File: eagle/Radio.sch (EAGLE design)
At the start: 105 parts, among them J500 2060-402, J501 2060-402, J920 2060-402, J921 2060-402, Q210 32.768kHz, Q610 32.768kHz, Q900 BSS123, U100 LP38693, U200 MSP430G2553, U300 IRF7103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

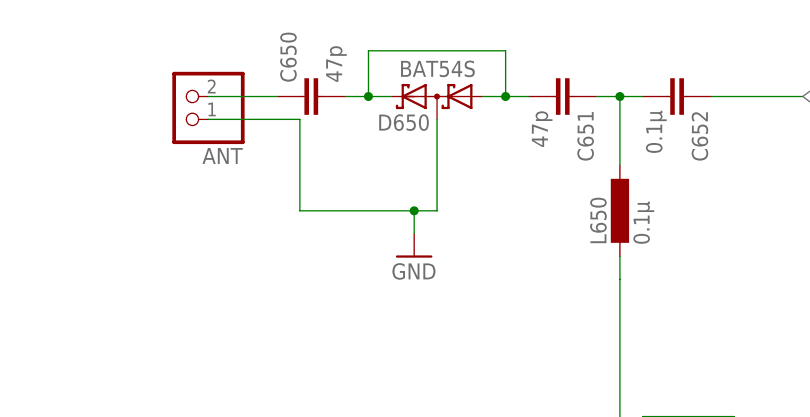
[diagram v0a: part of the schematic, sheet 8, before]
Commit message: CHG: eagle schemetics and layout to solve issue with diode on antenna
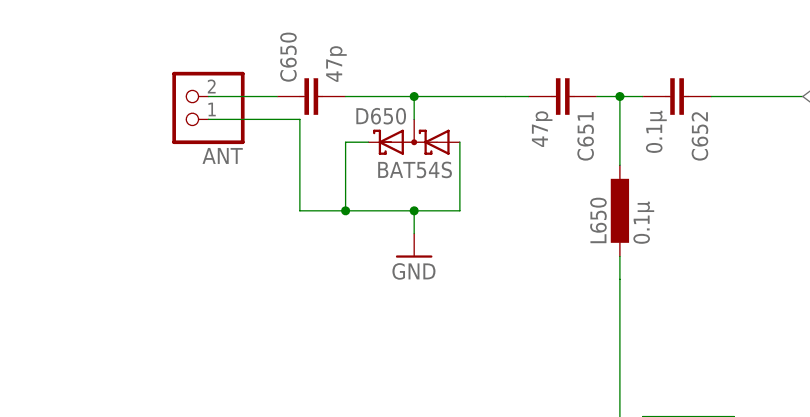
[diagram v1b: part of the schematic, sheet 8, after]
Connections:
- net GND: now also D650.A1, D650.C2; no longer D650.C1A2
- net N$2: now also D650.C1A2; no longer D650.A1, D650.C2
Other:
- moved on the sheet: D650
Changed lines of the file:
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@@
 <instance part="FRAME10" gate="G$1" x="0" y="0"/>
 <instance part="GND24" gate="1" x="167.64" y="93.98"/>
-<instance part="D650" gate="G$1" x="134.62" y="142.24" rot="R180"/>
+<instance part="D650" gate="G$1" x="132.08" y="137.16" rot="MR0"/>
 <instance part="ANT" gate="G$1" x="106.68" y="142.24" rot="R180"/>
 <instance part="C655" gate="G$1" x="165.1" y="78.74" rot="R270"/>
@@
 <net name="N$2" class="0">
 <segment>
+<pinref part="C651" gate="G$1" pin="2"/>
+<wire x1="144.78" y1="142.24" x2="142.24" y2="142.24" width="0.1524" layer="91"/>
 <pinref part="C650" gate="G$1" pin="2"/>
-<pinref part="D650" gate="G$1" pin="C2"/>
-<wire x1="124.46" y1="142.24" x2="127" y2="142.24" width="0.1524" layer="91"/>
-<wire x1="127" y1="142.24" x2="129.54" y2="142.24" width="0.1524" layer="91"/>
-<wire x1="127" y1="142.24" x2="127" y2="147.32" width="0.1524" layer="91"/>
-<junction x="127" y="142.24"/>
-<pinref part="C651" gate="G$1" pin="2"/>
-<pinref part="D650" gate="G$1" pin="A1"/>
-<wire x1="144.78" y1="142.24" x2="142.24" y2="142.24" width="0.1524" layer="91"/>
-<wire x1="142.24" y1="142.24" x2="139.7" y2="142.24" width="0.1524" layer="91"/>
-<wire x1="127" y1="147.32" x2="142.24" y2="147.32" width="0.1524" layer="91"/>
-<wire x1="142.24" y1="147.32" x2="142.24" y2="142.24" width="0.1524" layer="91"/>
-<junction x="142.24" y="142.24"/>
+<pinref part="D650" gate="G$1" pin="C1A2"/>
+<wire x1="124.46" y1="142.24" x2="132.08" y2="142.24" width="0.1524" layer="91"/>
+<wire x1="132.08" y1="142.24" x2="132.08" y2="139.7" width="0.1524" layer="91"/>
+<wire x1="142.24" y1="142.24" x2="132.08" y2="142.24" width="0.1524" layer="91"/>
+<junction x="132.08" y="142.24"/>
 </segment>
 </net>
@@
 </segment>
 <segment>
-<pinref part="D650" gate="G$1" pin="C1A2"/>
-<wire x1="134.62" y1="139.7" x2="134.62" y2="129.54" width="0.1524" layer="91"/>
 <pinref part="GND37" gate="1" pin="GND"/>
-<wire x1="134.62" y1="129.54" x2="132.08" y2="129.54" width="0.1524" layer="91"/>
 <wire x1="132.08" y1="129.54" x2="132.08" y2="127" width="0.1524" layer="91"/>
 <pinref part="ANT" gate="G$1" pin="1"/>
 <wire x1="119.38" y1="139.7" x2="109.22" y2="139.7" width="0.1524" layer="91"/>
 <wire x1="119.38" y1="139.7" x2="119.38" y2="129.54" width="0.1524" layer="91"/>
-<wire x1="119.38" y1="129.54" x2="132.08" y2="129.54" width="0.1524" layer="91"/>
+<wire x1="119.38" y1="129.54" x2="124.46" y2="129.54" width="0.1524" layer="91"/>
+<pinref part="D650" gate="G$1" pin="C2"/>
+<wire x1="124.46" y1="129.54" x2="132.08" y2="129.54" width="0.1524" layer="91"/>
+<wire x1="127" y1="137.16" x2="124.46" y2="137.16" width="0.1524" layer="91"/>
+<wire x1="124.46" y1="137.16" x2="124.46" y2="129.54" width="0.1524" layer="91"/>
+<junction x="124.46" y="129.54"/>
+<pinref part="D650" gate="G$1" pin="A1"/>
+<wire x1="137.16" y1="137.16" x2="137.16" y2="129.54" width="0.1524" layer="91"/>
+<wire x1="137.16" y1="129.54" x2="132.08" y2="129.54" width="0.1524" layer="91"/>
 <junction x="132.08" y="129.54"/>
 </segment>

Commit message: CHG: Finishing Layout and Schemetics
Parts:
- added R921, R922, R923: 1k, rcl:R-EU_R1206
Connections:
- new net N$25: R921.1, U920.LED1
- new net N$45: J920.B-2, R922.2
- new net N$46: J921.B-2, R923.2
- net +5V: no longer R901.1
- net GND: now also R901.1
- net N$3: now also R923.1, U920.LED3; no longer J920.B-1, U920.LED1
- net N$44: now also J920.B-1, R921.2; no longer J921.B-2, U920.LED3
- net N$5: now also R922.1; no longer J920.B-2
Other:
- moved on the sheet: J920, J921
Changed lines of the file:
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@@
 <part name="GND28" library="supply1" deviceset="GND" device=""/>
 <part name="R901" library="rcl" deviceset="R-EU_" device="R1206" value="1k"/>
-<part name="P+2" library="supply1" deviceset="+5V" device=""/>
 <part name="J501" library="Wago-2060-402" deviceset="2060-402" device=""/>
 <part name="J500" library="Wago-2060-402" deviceset="2060-402" device=""/>
@@
 <part name="J920" library="Wago-2060-402" deviceset="2060-402" device=""/>
 <part name="U940" library="Radio Projekt" deviceset="OPT3001" device=""/>
+<part name="GND25" library="supply1" deviceset="GND" device=""/>
+<part name="R921" library="rcl" deviceset="R-EU_" device="R1206" value="1k"/>
+<part name="R922" library="rcl" deviceset="R-EU_" device="R1206" value="1k"/>
+<part name="R923" library="rcl" deviceset="R-EU_" device="R1206" value="1k"/>
 </parts>
 <sheets>
@@
 <instance part="GND28" gate="1" x="137.16" y="104.14"/>
 <instance part="R901" gate="G$1" x="149.86" y="119.38" rot="R270"/>
-<instance part="P+2" gate="1" x="149.86" y="129.54"/>
-<instance part="J921" gate="A" x="101.6" y="30.48" rot="MR180"/>
-<instance part="P+4" gate="1" x="93.98" y="10.16" rot="R180"/>
+<instance part="J921" gate="A" x="116.84" y="30.48" rot="MR180"/>
+<instance part="P+4" gate="1" x="109.22" y="10.16" rot="R180"/>
 <instance part="C903" gate="G$1" x="127" y="142.24" rot="R90"/>
 <instance part="GND32" gate="1" x="139.7" y="142.24" rot="R90"/>
@@
 <instance part="U920" gate="G$1" x="68.58" y="43.18"/>
 <instance part="GND39" gate="1" x="45.72" y="27.94"/>
-<instance part="J920" gate="A" x="101.6" y="45.72"/>
+<instance part="J920" gate="A" x="116.84" y="45.72"/>
+<instance part="GND25" gate="1" x="149.86" y="129.54" rot="R180"/>
+<instance part="R921" gate="G$1" x="93.98" y="45.72"/>
+<instance part="R922" gate="G$1" x="101.6" y="38.1"/>
+<instance part="R923" gate="G$1" x="93.98" y="33.02"/>
 </instances>
 <busses>
@@
 <wire x1="45.72" y1="30.48" x2="45.72" y2="33.02" width="0.1524" layer="91"/>
 <wire x1="45.72" y1="33.02" x2="50.8" y2="33.02" width="0.1524" layer="91"/>
+</segment>
+<segment>
+<pinref part="R901" gate="G$1" pin="1"/>
+<wire x1="149.86" y1="124.46" x2="149.86" y2="127" width="0.1524" layer="91"/>
+<pinref part="GND25" gate="1" pin="GND"/>
 </segment>
 </net>
@@
 </segment>
 <segment>
-<pinref part="R901" gate="G$1" pin="1"/>
-<pinref part="P+2" gate="1" pin="+5V"/>
-<wire x1="149.86" y1="124.46" x2="149.86" y2="127" width="0.1524" layer="91"/>
-</segment>
-<segment>
-<wire x1="93.98" y1="15.24" x2="93.98" y2="12.7" width="0.1524" layer="91"/>
+<wire x1="109.22" y1="17.78" x2="109.22" y2="12.7" width="0.1524" layer="91"/>
 <pinref part="P+4" gate="1" pin="+5V"/>
-<wire x1="93.98" y1="25.4" x2="93.98" y2="30.48" width="0.1524" layer="91"/>
+<wire x1="109.22" y1="25.4" x2="109.22" y2="30.48" width="0.1524" layer="91"/>
 <pinref part="J921" gate="A" pin="B-1"/>
-<wire x1="96.52" y1="30.48" x2="93.98" y2="30.48" width="0.1524" layer="91"/>
-<wire x1="93.98" y1="15.24" x2="93.98" y2="25.4" width="0.1524" layer="91"/>
+<wire x1="111.76" y1="30.48" x2="109.22" y2="30.48" width="0.1524" layer="91"/>
+<wire x1="109.22" y1="17.78" x2="109.22" y2="25.4" width="0.1524" layer="91"/>
 </segment>
 <segment>
@@
 <net name="N$3" class="0">
 <segment>
+<pinref part="U920" gate="G$1" pin="LED3"/>
+<pinref part="R923" gate="G$1" pin="1"/>
+<wire x1="86.36" y1="33.02" x2="88.9" y2="33.02" width="0.1524" layer="91"/>
+</segment>
+</net>
+<net name="N$5" class="0">
+<segment>
+<pinref part="U920" gate="G$1" pin="LED2"/>
+<pinref part="R922" gate="G$1" pin="1"/>
+<wire x1="86.36" y1="38.1" x2="96.52" y2="38.1" width="0.1524" layer="91"/>
+</segment>
+</net>
+<net name="N$25" class="0">
+<segment>
 <pinref part="U920" gate="G$1" pin="LED1"/>
+<pinref part="R921" gate="G$1" pin="1"/>
+<wire x1="86.36" y1="45.72" x2="88.9" y2="45.72" width="0.1524" layer="91"/>
+</segment>
+</net>
+<net name="N$44" class="0">
+<segment>
+<pinref part="R921" gate="G$1" pin="2"/>
 <pinref part="J920" gate="A" pin="B-1"/>
-<wire x1="86.36" y1="45.72" x2="96.52" y2="45.72" width="0.1524" layer="91"/>
-</segment>
-</net>
-<net name="N$5" class="0">
-<segment>
-<pinref part="U920" gate="G$1" pin="LED2"/>
-<wire x1="86.36" y1="38.1" x2="91.44" y2="38.1" width="0.1524" layer="91"/>
+<wire x1="99.06" y1="45.72" x2="111.76" y2="45.72" width="0.1524" layer="91"/>
+</segment>
+</net>
+<net name="N$45" class="0">
+<segment>
+<pinref part="R922" gate="G$1" pin="2"/>
+<wire x1="106.68" y1="38.1" x2="109.22" y2="38.1" width="0.1524" layer="91"/>
+<wire x1="109.22" y1="38.1" x2="109.22" y2="43.18" width="0.1524" layer="91"/>
 <pinref part="J920" gate="A" pin="B-2"/>
-<wire x1="91.44" y1="38.1" x2="91.44" y2="43.18" width="0.1524" layer="91"/>
-<wire x1="91.44" y1="43.18" x2="96.52" y2="43.18" width="0.1524" layer="91"/>
-</segment>
-</net>
-<net name="N$44" class="0">
-<segment>
-<pinref part="U920" gate="G$1" pin="LED3"/>
+<wire x1="109.22" y1="43.18" x2="111.76" y2="43.18" width="0.1524" layer="91"/>
+</segment>
+</net>
+<net name="N$46" class="0">
+<segment>
+<pinref part="R923" gate="G$1" pin="2"/>
 <pinref part="J921" gate="A" pin="B-2"/>
-<wire x1="86.36" y1="33.02" x2="96.52" y2="33.02" width="0.1524" layer="91"/>
-</segment>
-</net>
+<wire x1="99.06" y1="33.02" x2="111.76" y2="33.02" width="0.1524" layer="91"/>
+</segment>
+</net>

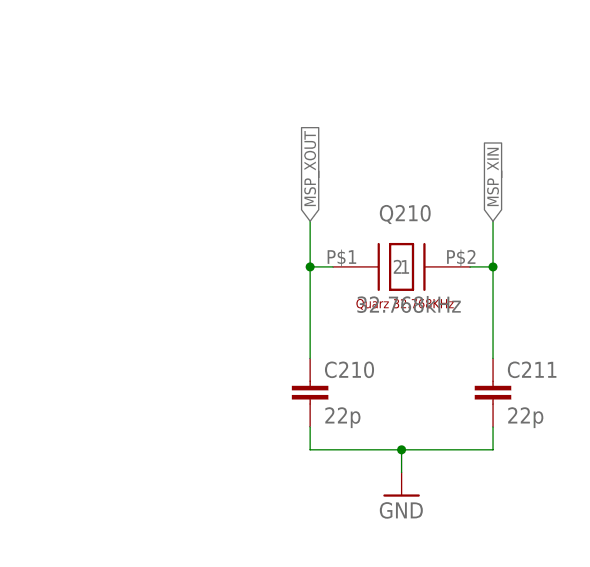
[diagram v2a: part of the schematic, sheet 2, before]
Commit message: CHG: solved some problems on pcb updated encoder footprint, further updated schemetics and changed pull up resitor to an pull down for lcd backlight controll
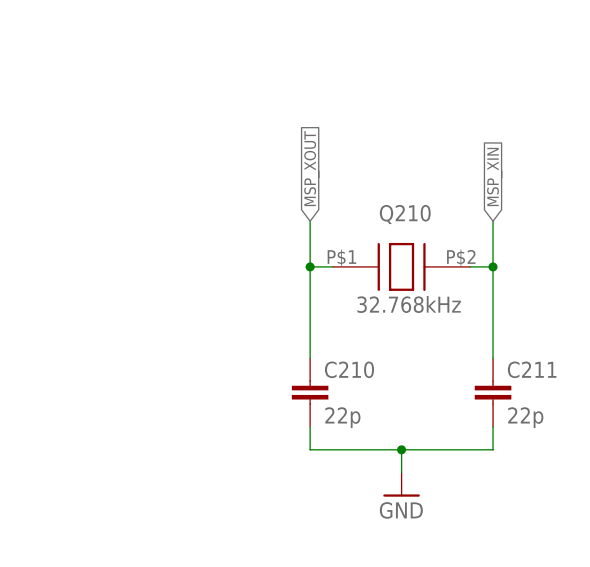
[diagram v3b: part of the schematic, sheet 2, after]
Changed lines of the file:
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@@
 <grid distance="0.1" unitdist="inch" unit="inch" style="lines" multiple="1" display="no" altdistance="0.01" altunitdist="inch" altunit="inch"/>
 <layers>
-<layer number="1" name="Top" color="4" fill="1" visible="no" active="no"/>
-<layer number="2" name="Route2" color="1" fill="3" visible="no" active="no"/>
-<layer number="3" name="Route3" color="4" fill="3" visible="no" active="no"/>
-<layer number="4" name="Route4" color="1" fill="4" visible="no" active="no"/>
-<layer number="5" name="Route5" color="4" fill="4" visible="no" active="no"/>
-<layer number="6" name="Route6" color="1" fill="8" visible="no" active="no"/>
-<layer number="7" name="Route7" color="4" fill="8" visible="no" active="no"/>
-<layer number="8" name="Route8" color="1" fill="2" visible="no" active="no"/>
-<layer number="9" name="Route9" color="4" fill="2" visible="no" active="no"/>
-<layer number="10" name="Route10" color="1" fill="7" visible="no" active="no"/>
-<layer number="11" name="Route11" color="4" fill="7" visible="no" active="no"/>
-<layer number="12" name="Route12" color="1" fill="5" visible="no" active="no"/>
-<layer number="13" name="Route13" color="4" fill="5" visible="no" active="no"/>
-<layer number="14" name="Route14" color="1" fill="6" visible="no" active="no"/>
-<layer number="15" name="Route15" color="4" fill="6" visible="no" active="no"/>
-<layer number="16" name="Bottom" color="1" fill="1" visible="no" active="no"/>
-<layer number="17" name="Pads" color="2" fill="1" visible="no" active="no"/>
-<layer number="18" name="Vias" color="2" fill="1" visible="no" active="no"/>
-<layer number="19" name="Unrouted" color="6" fill="1" visible="no" active="no"/>
-<layer number="20" name="Dimension" color="15" fill="1" visible="no" active="no"/>
-<layer number="21" name="tPlace" color="7" fill="1" visible="no" active="no"/>
-<layer number="22" name="bPlace" color="7" fill="1" visible="no" active="no"/>
-<layer number="23" name="tOrigins" color="15" fill="1" visible="no" active="no"/>
-<layer number="24" name="bOrigins" color="15" fill="1" visible="no" active="no"/>
-<layer number="25" name="tNames" color="7" fill="1" visible="no" active="no"/>
-<layer number="26" name="bNames" color="7" fill="1" visible="no" active="no"/>
-<layer number="27" name="tValues" color="7" fill="1" visible="no" active="no"/>
-<layer number="28" name="bValues" color="7" fill="1" visible="no" active="no"/>
+<layer number="1" name="Top" color="4" fill="1" visible="yes" active="no"/>
+<layer number="2" name="Route2" color="1" fill="3" visible="yes" active="no"/>
+<layer number="3" name="Route3" color="4" fill="3" visible="yes" active="no"/>
+<layer number="4" name="Route4" color="1" fill="4" visible="yes" active="no"/>
+<layer number="5" name="Route5" color="4" fill="4" visible="yes" active="no"/>
+<layer number="6" name="Route6" color="1" fill="8" visible="yes" active="no"/>
+<layer number="7" name="Route7" color="4" fill="8" visible="yes" active="no"/>
+<layer number="8" name="Route8" color="1" fill="2" visible="yes" active="no"/>
+<layer number="9" name="Route9" color="4" fill="2" visible="yes" active="no"/>
+<layer number="10" name="Route10" color="1" fill="7" visible="yes" active="no"/>
+<layer number="11" name="Route11" color="4" fill="7" visible="yes" active="no"/>
+<layer number="12" name="Route12" color="1" fill="5" visible="yes" active="no"/>
+<layer number="13" name="Route13" color="4" fill="5" visible="yes" active="no"/>
+<layer number="14" name="Route14" color="1" fill="6" visible="yes" active="no"/>
+<layer number="15" name="Route15" color="4" fill="6" visible="yes" active="no"/>
+<layer number="16" name="Bottom" color="1" fill="1" visible="yes" active="no"/>
+<layer number="17" name="Pads" color="2" fill="1" visible="yes" active="no"/>
+<layer number="18" name="Vias" color="2" fill="1" visible="yes" active="no"/>
+<layer number="19" name="Unrouted" color="6" fill="1" visible="yes" active="no"/>
+<layer number="20" name="Dimension" color="15" fill="1" visible="yes" active="no"/>
+<layer number="21" name="tPlace" color="7" fill="1" visible="yes" active="no"/>
+<layer number="22" name="bPlace" color="7" fill="1" visible="yes" active="no"/>
+<layer number="23" name="tOrigins" color="15" fill="1" visible="yes" active="no"/>
+<layer number="24" name="bOrigins" color="15" fill="1" visible="yes" active="no"/>
+<layer number="25" name="tNames" color="7" fill="1" visible="yes" active="no"/>
+<layer number="26" name="bNames" color="7" fill="1" visible="yes" active="no"/>
+<layer number="27" name="tValues" color="7" fill="1" visible="yes" active="no"/>
+<layer number="28" name="bValues" color="7" fill="1" visible="yes" active="no"/>
 <layer number="29" name="tStop" color="7" fill="3" visible="no" active="no"/>
 <layer number="30" name="bStop" color="7" fill="6" visible="no" active="no"/>
@@
 <layer number="35" name="tGlue" color="7" fill="4" visible="no" active="no"/>
 <layer number="36" name="bGlue" color="7" fill="5" visible="no" active="no"/>
-<layer number="37" name="tTest" color="7" fill="1" visible="no" active="no"/>
-<layer number="38" name="bTest" color="7" fill="1" visible="no" active="no"/>
+<layer number="37" name="tTest" color="7" fill="1" visible="yes" active="no"/>
+<layer number="38" name="bTest" color="7" fill="1" visible="yes" active="no"/>
 <layer number="39" name="tKeepout" color="4" fill="11" visible="no" active="no"/>
 <layer number="40" name="bKeepout" color="1" fill="11" visible="no" active="no"/>
@@
 <layer number="44" name="Drills" color="7" fill="1" visible="no" active="no"/>
 <layer number="45" name="Holes" color="7" fill="1" visible="no" active="no"/>
-<layer number="46" name="Milling" color="3" fill="1" visible="no" active="no"/>
-<layer number="47" name="Measures" color="7" fill="1" visible="no" active="no"/>
-<layer number="48" name="Document" color="7" fill="1" visible="no" active="no"/>
-<layer number="49" name="Reference" color="7" fill="1" visible="no" active="no"/>
-<layer number="50" name="dxf" color="7" fill="1" visible="no" active="no"/>
-<layer number="51" name="tDocu" color="7" fill="1" visible="no" active="no"/>
-<layer number="52" name="bDocu" color="7" fill="1" visible="no" active="no"/>
-<layer number="53" name="tCopper" color="7" fill="11" visible="no" active="no"/>
-<layer number="54" name="bCopper" color="7" fill="1" visible="no" active="no"/>
-<layer number="56" name="wert" color="7" fill="1" visible="no" active="no"/>
+<layer number="46" name="Milling" color="3" fill="1" visible="yes" active="no"/>
+<layer number="47" name="Measures" color="7" fill="1" visible="yes" active="no"/>
+<layer number="48" name="Document" color="7" fill="1" visible="yes" active="no"/>
+<layer number="49" name="Reference" color="7" fill="1" visible="yes" active="no"/>
+<layer number="50" name="dxf" color="7" fill="1" visible="yes" active="no"/>
+<layer number="51" name="tDocu" color="7" fill="1" visible="yes" active="no"/>
+<layer number="52" name="bDocu" color="7" fill="1" visible="yes" active="no"/>
+<layer number="53" name="tCopper" color="7" fill="11" visible="yes" active="no"/>
+<layer number="54" name="bCopper" color="7" fill="1" visible="yes" active="no"/>
+<layer number="56" name="wert" color="7" fill="1" visible="yes" active="no"/>
 <layer number="91" name="Nets" color="2" fill="1" visible="yes" active="yes"/>
 <layer number="92" name="Busses" color="1" fill="1" visible="yes" active="yes"/>

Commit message: CHG: updated radio schematics and pcb with test pads
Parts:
- added TP1, TP10, TP11, TP12, TP13, TP14, TP15, TP16, TP17, TP2, TP27, TP28, TP3, TP9: PTR1B1,27, testpad:PTR1B1,27
- added TP23, TP24, TP25, TP26, TP29, TP30, TP31, TP4, TP5, TP6, TP7, TP8: PTR1B2,54, testpad:PTR1B2,54
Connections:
- removed net N$13: C510.2, J500.B-1, L510.1
- removed net N$14: C511.2, J500.B-2, L511.1
- removed net N$15: C512.1, J501.B-2, L512.1
- removed net N$16: C513.1, J501.B-1, L513.1
- removed net N$41: ANT.2, C650.1
- new net AMP_OUTL+: C510.2, J500.B-1, L510.1, TP25.TP
- new net AMP_OUTL-: C511.2, J500.B-2, L511.1, TP26.TP
- new net AMP_OUTR+: C512.1, J501.B-2, L512.1, TP23.TP
- new net AMP_OUTR-: C513.1, J501.B-1, L513.1, TP24.TP
- new net ANT_FM: ANT.2, C650.1, TP13.TP
- net +3V3: now also TP1.TP
- net +5V: now also TP2.TP, TP29.TP, TP3.TP, TP31.TP
- net AMP_LIN: now also TP16.TP
- net AMP_RIN: now also TP17.TP
- net AUX_LIN: now also TP14.TP
- net AUX_RIN: now also TP15.TP
- net GND: now also TP30.TP, TP4.TP, TP5.TP, TP6.TP, TP7.TP, TP8.TP
- net SCL_3.3V: now also TP10.TP
- net SCL_5V: now also TP28.TP
- net SDA_3.3V: now also TP9.TP
- net SDA_5V: now also TP27.TP
- net SI_LOUT: now also TP11.TP
- net SI_ROUT: now also TP12.TP
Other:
- note added: "Testpads"
